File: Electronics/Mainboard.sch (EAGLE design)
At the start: 14 parts, among them IC1 4081N, T1 BC547, T2 BC547

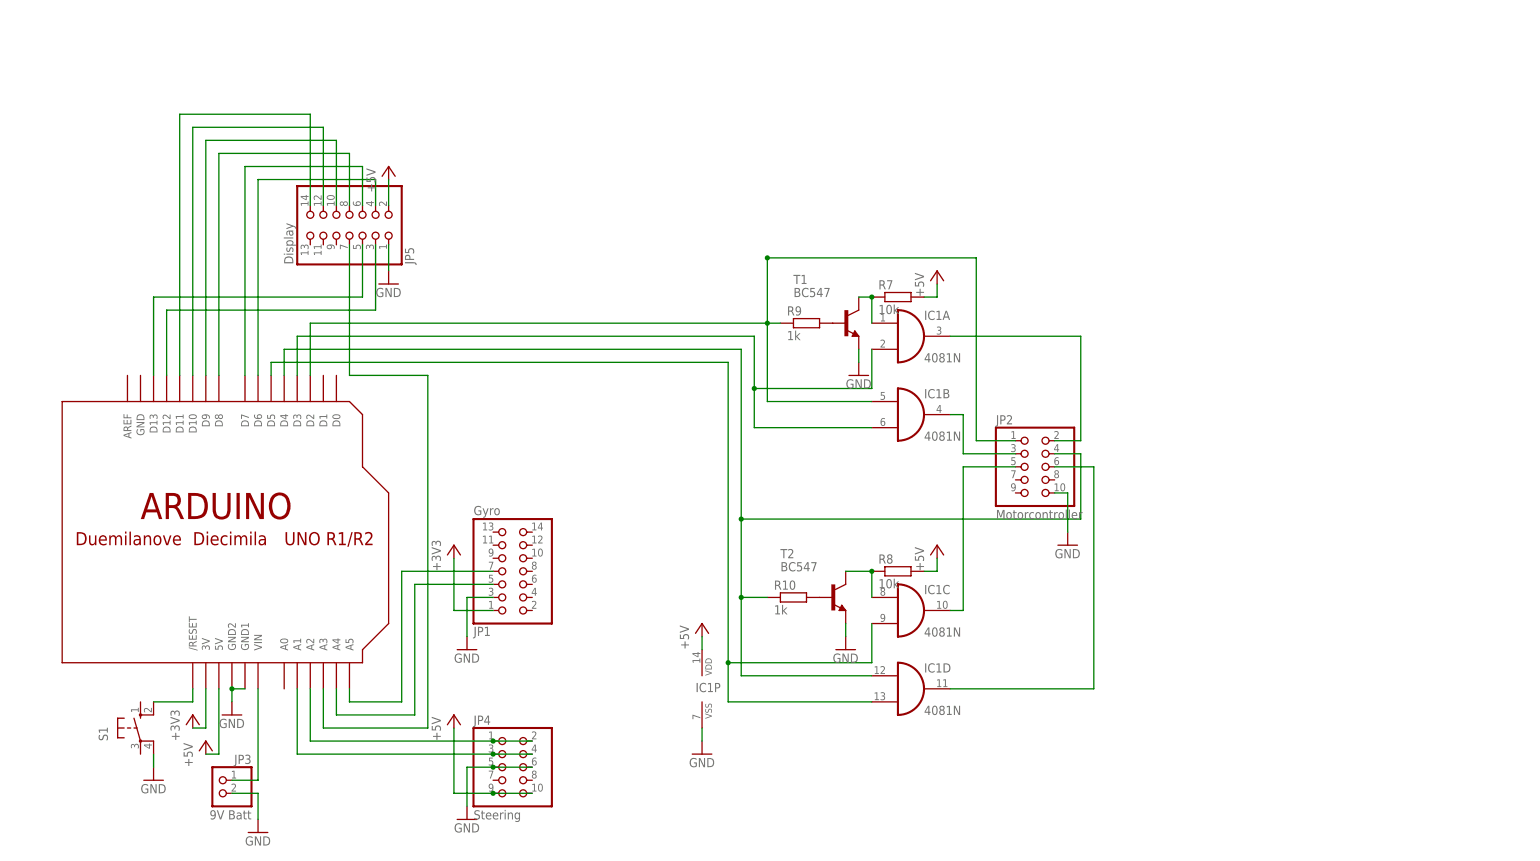
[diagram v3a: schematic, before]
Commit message: New mainboard. Closes #13, closes #21 and closes #9 as it becomes irrelevant.
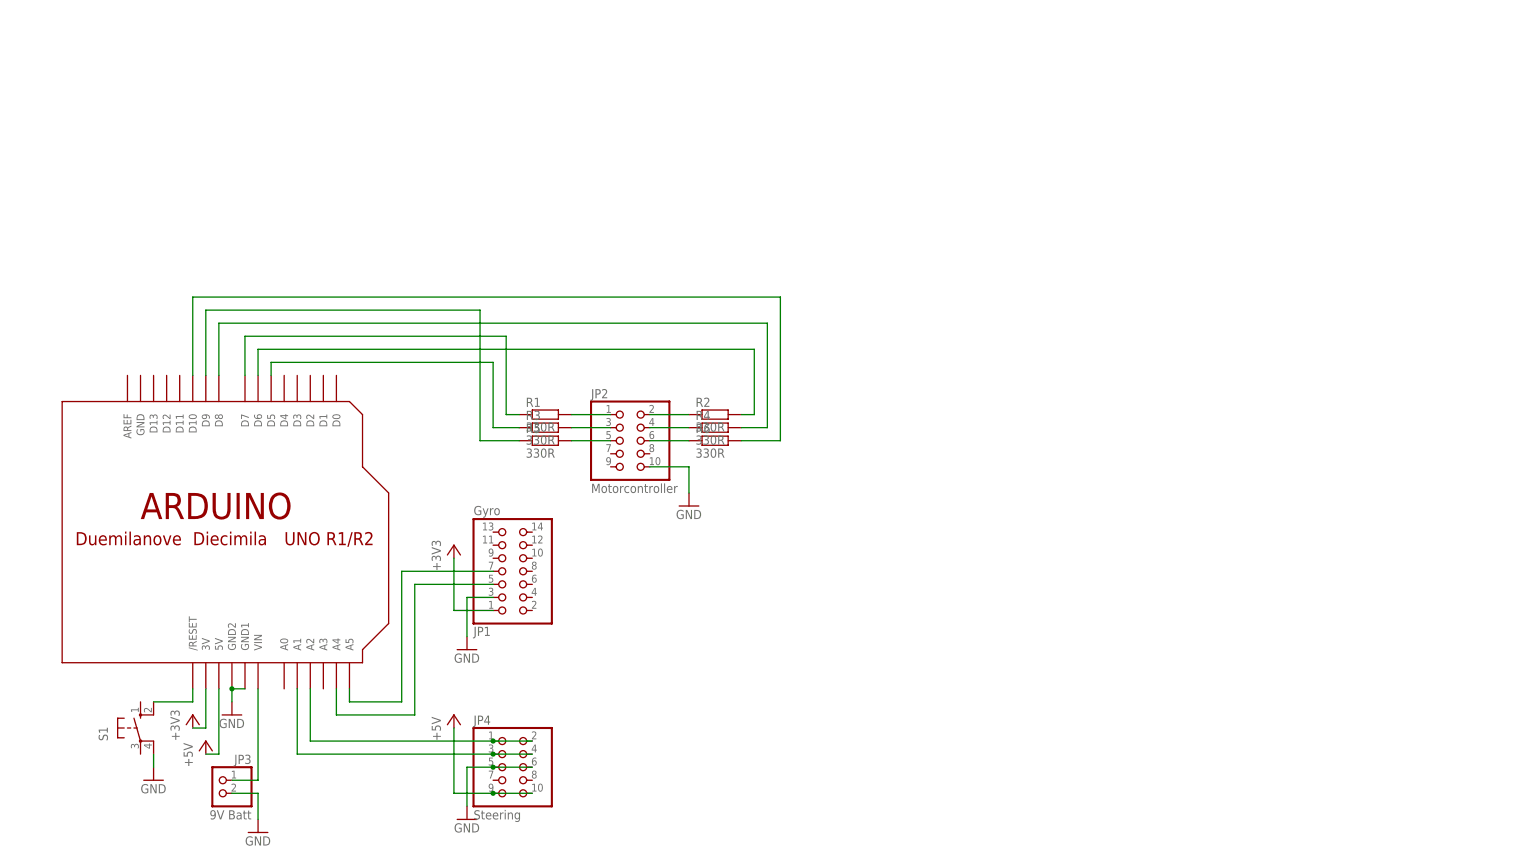
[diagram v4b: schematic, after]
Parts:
- removed IC1: 4081N, 40xx:4081N
- removed JP5: Display, pinhead:PINHD-2X7
- removed R10, R9: 1k, rcl:R-EU_0207/10
- removed R7, R8: 10k, rcl:R-EU_0207/10
- removed T1, T2: BC547, transistor:BC547
- added R1, R2, R3, R4, R5, R6: 330R, rcl:R-EU_0207/10
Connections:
- removed net N$20: R10.2, T2.B
- removed net N$31: JP5.4, U$1.D6
- removed net N$37: JP5.6, U$1.D7
- removed net N$38: JP5.8, U$1.D8
- removed net N$40: JP5.10, U$1.D9
- removed net N$42: JP5.12, U$1.D10
- removed net N$43: JP5.14, U$1.D11
- removed net N$44: JP5.3, U$1.D12
- removed net N$45: JP5.5, U$1.D13
- removed net N$46: JP5.7, U$1.A3
- new net N$6: JP2.6, R6.1
- net +5V: no longer IC1P.VDD, JP5.2, R7.2, R8.2
- net GND: no longer IC1P.VSS, JP5.1, T1.E, T2.E
- net N$1: now also JP2.1, R1.2; no longer IC1A.O, JP2.2
- net N$10: now also R2.2, U$1.D6; no longer IC1B.I0, JP2.1, R9.1, U$1.D2
- net N$11: now also R4.2, U$1.D8; no longer IC1A.I1, IC1B.I1, U$1.D3
- net N$16: now also R5.1, U$1.D9; no longer IC1C.I0, R8.1, T2.C
- net N$17: now also R6.2, U$1.D10; no longer R9.2, T1.B
- net N$2: now also R3.2; no longer IC1B.O
- net N$3: now also JP2.5, R5.2; no longer IC1D.I0, JP2.4, R10.1, U$1.D4
- net N$4: now also JP2.2, R2.1; no longer IC1C.O, JP2.5
- net N$5: now also JP2.4, R4.1; no longer IC1D.O, JP2.6
- net N$7: now also R1.1, U$1.D7; no longer IC1C.I1, IC1D.I1, U$1.D5
- net N$8: now also R3.1, U$1.D5; no longer IC1A.I0, R7.1, T1.C
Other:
- moved on the sheet: JP2

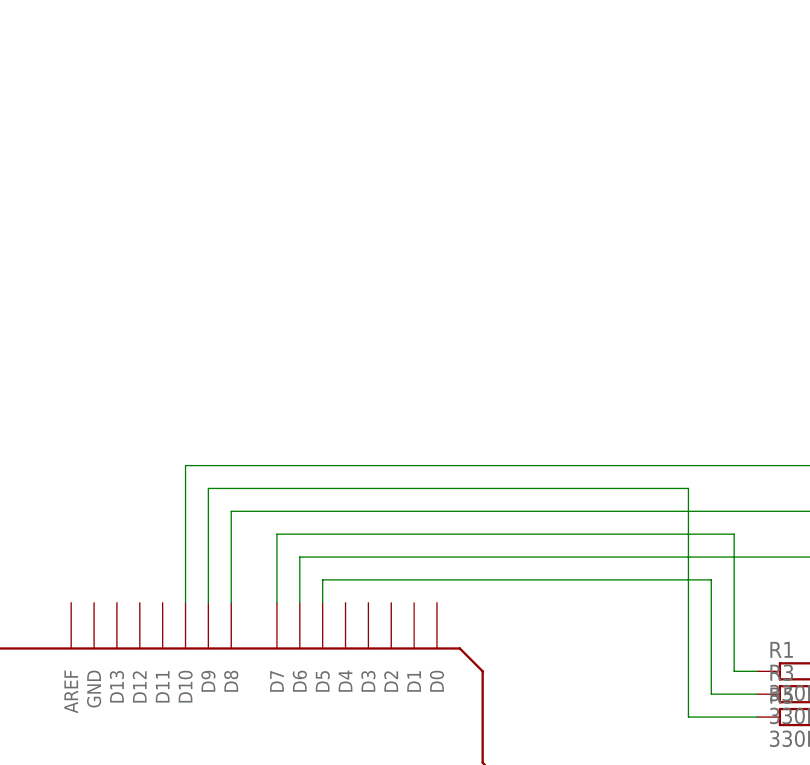
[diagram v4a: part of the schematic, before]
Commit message: Radio on mainboard. Closes #29
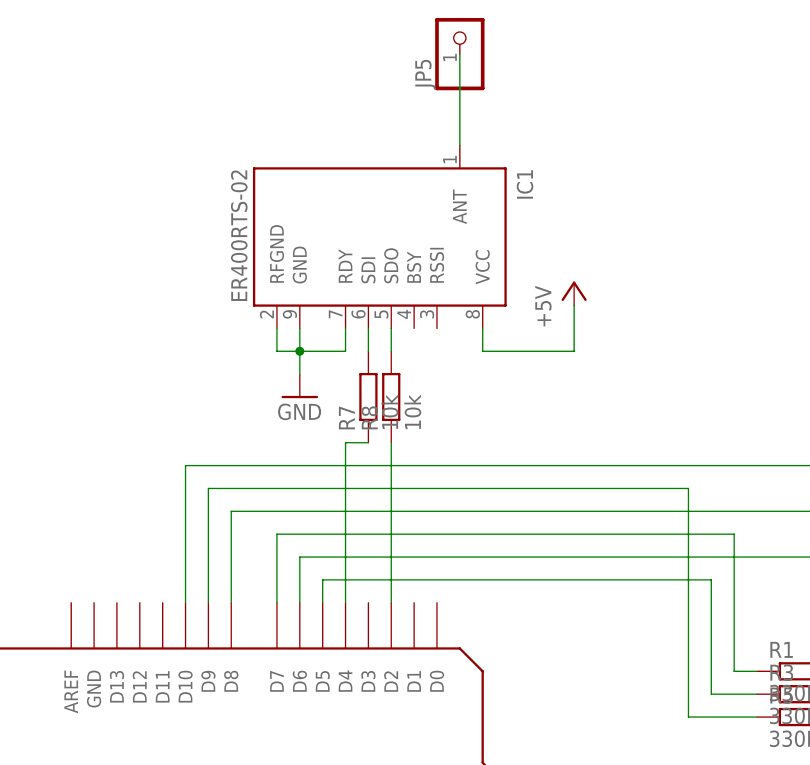
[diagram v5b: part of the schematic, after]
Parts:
- added IC1: ER400RTS-02, lprs:ER400RTS-02
- added JP5: (no value), adafruit:PINHD-1X1
- added R7, R8: 10k, rcl:R-EU_0207/10
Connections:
- new net N$12: R7.1, U$1.D4
- new net N$18: IC1.SDO, R8.2
- new net N$19: IC1.SDI, R7.2
- new net N$21: IC1.ANT, JP5.1
- new net N$9: R8.1, U$1.D2
- net +5V: now also IC1.VCC
- net GND: now also IC1.GND, IC1.RDY, IC1.RFGND
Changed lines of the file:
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@@
 <part name="R5" library="rcl" deviceset="R-EU_" device="0207/10" value="330R"/>
 <part name="R6" library="rcl" deviceset="R-EU_" device="0207/10" value="330R"/>
+<part name="IC1" library="lprs" deviceset="ER*00RTS-02" device="" technology="4"/>
+<part name="GND4" library="supply1" deviceset="GND" device=""/>
+<part name="R7" library="rcl" deviceset="R-EU_" device="0207/10" value="10k"/>
+<part name="R8" library="rcl" deviceset="R-EU_" device="0207/10" value="10k"/>
+<part name="P+1" library="supply1" deviceset="+5V" device=""/>
+<part name="JP5" library="adafruit" deviceset="PINHD-1X1" device=""/>
 </parts>
 <sheets>
@@
 <instance part="R5" gate="G$1" x="60.96" y="88.9"/>
 <instance part="R6" gate="G$1" x="93.98" y="88.9"/>
+<instance part="IC1" gate="G$1" x="12.7" y="142.24" rot="R270"/>
+<instance part="GND4" gate="1" x="5.08" y="124.46"/>
+<instance part="R7" gate="G$1" x="12.7" y="124.46" rot="R90"/>
+<instance part="R8" gate="G$1" x="15.24" y="124.46" rot="R90"/>
+<instance part="P+1" gate="1" x="35.56" y="137.16"/>
+<instance part="JP5" gate="G$1" x="22.86" y="165.1" rot="R90"/>
 </instances>
 <busses>
@@
 <wire x1="-15.24" y1="25.4" x2="-15.24" y2="27.94" width="0.1524" layer="91"/>
 </segment>
+<segment>
+<pinref part="GND4" gate="1" pin="GND"/>
+<pinref part="IC1" gate="G$1" pin="GND"/>
+<wire x1="5.08" y1="127" x2="5.08" y2="129.54" width="0.1524" layer="91"/>
+<wire x1="5.08" y1="129.54" x2="5.08" y2="132.08" width="0.1524" layer="91"/>
+<pinref part="IC1" gate="G$1" pin="RDY"/>
+<wire x1="10.16" y1="132.08" x2="10.16" y2="129.54" width="0.1524" layer="91"/>
+<wire x1="10.16" y1="129.54" x2="5.08" y2="129.54" width="0.1524" layer="91"/>
+<junction x="5.08" y="129.54"/>
+<pinref part="IC1" gate="G$1" pin="RFGND"/>
+<wire x1="2.54" y1="132.08" x2="2.54" y2="129.54" width="0.1524" layer="91"/>
+<wire x1="2.54" y1="129.54" x2="5.08" y2="129.54" width="0.1524" layer="91"/>
+</segment>
 </net>
 <net name="N$26" class="0">
@@
 <junction x="50.8" y="20.32"/>
 </segment>
+<segment>
+<pinref part="IC1" gate="G$1" pin="VCC"/>
+<wire x1="25.4" y1="132.08" x2="25.4" y2="129.54" width="0.1524" layer="91"/>
+<wire x1="25.4" y1="129.54" x2="35.56" y2="129.54" width="0.1524" layer="91"/>
+<pinref part="P+1" gate="1" pin="+5V"/>
+<wire x1="35.56" y1="129.54" x2="35.56" y2="134.62" width="0.1524" layer="91"/>
+</segment>
 </net>
 <net name="N$13" class="0">
@@
 </segment>
 </net>
+<net name="N$12" class="0">
+<segment>
+<wire x1="12.7" y1="119.38" x2="10.16" y2="119.38" width="0.1524" layer="91"/>
+<pinref part="U$1" gate="G$1" pin="D4"/>
+<wire x1="10.16" y1="119.38" x2="10.16" y2="101.6" width="0.1524" layer="91"/>
+<pinref part="R7" gate="G$1" pin="1"/>
+</segment>
+</net>
+<net name="N$9" class="0">
+<segment>
+<pinref part="U$1" gate="G$1" pin="D2"/>
+<pinref part="R8" gate="G$1" pin="1"/>
+<wire x1="15.24" y1="101.6" x2="15.24" y2="119.38" width="0.1524" layer="91"/>
+</segment>
+</net>
+<net name="N$18" class="0">
+<segment>
+<pinref part="R8" gate="G$1" pin="2"/>
+<pinref part="IC1" gate="G$1" pin="SDO"/>
+<wire x1="15.24" y1="129.54" x2="15.24" y2="132.08" width="0.1524" layer="91"/>
+</segment>
+</net>
+<net name="N$19" class="0">
+<segment>
+<pinref part="R7" gate="G$1" pin="2"/>
+<pinref part="IC1" gate="G$1" pin="SDI"/>
+<wire x1="12.7" y1="129.54" x2="12.7" y2="132.08" width="0.1524" layer="91"/>
+</segment>
+</net>
+<net name="N$21" class="0">
+<segment>
+<pinref part="JP5" gate="G$1" pin="1"/>
+<pinref part="IC1" gate="G$1" pin="ANT"/>
+<wire x1="22.86" y1="162.56" x2="22.86" y2="152.4" width="0.1524" layer="91"/>
+</segment>
+</net>

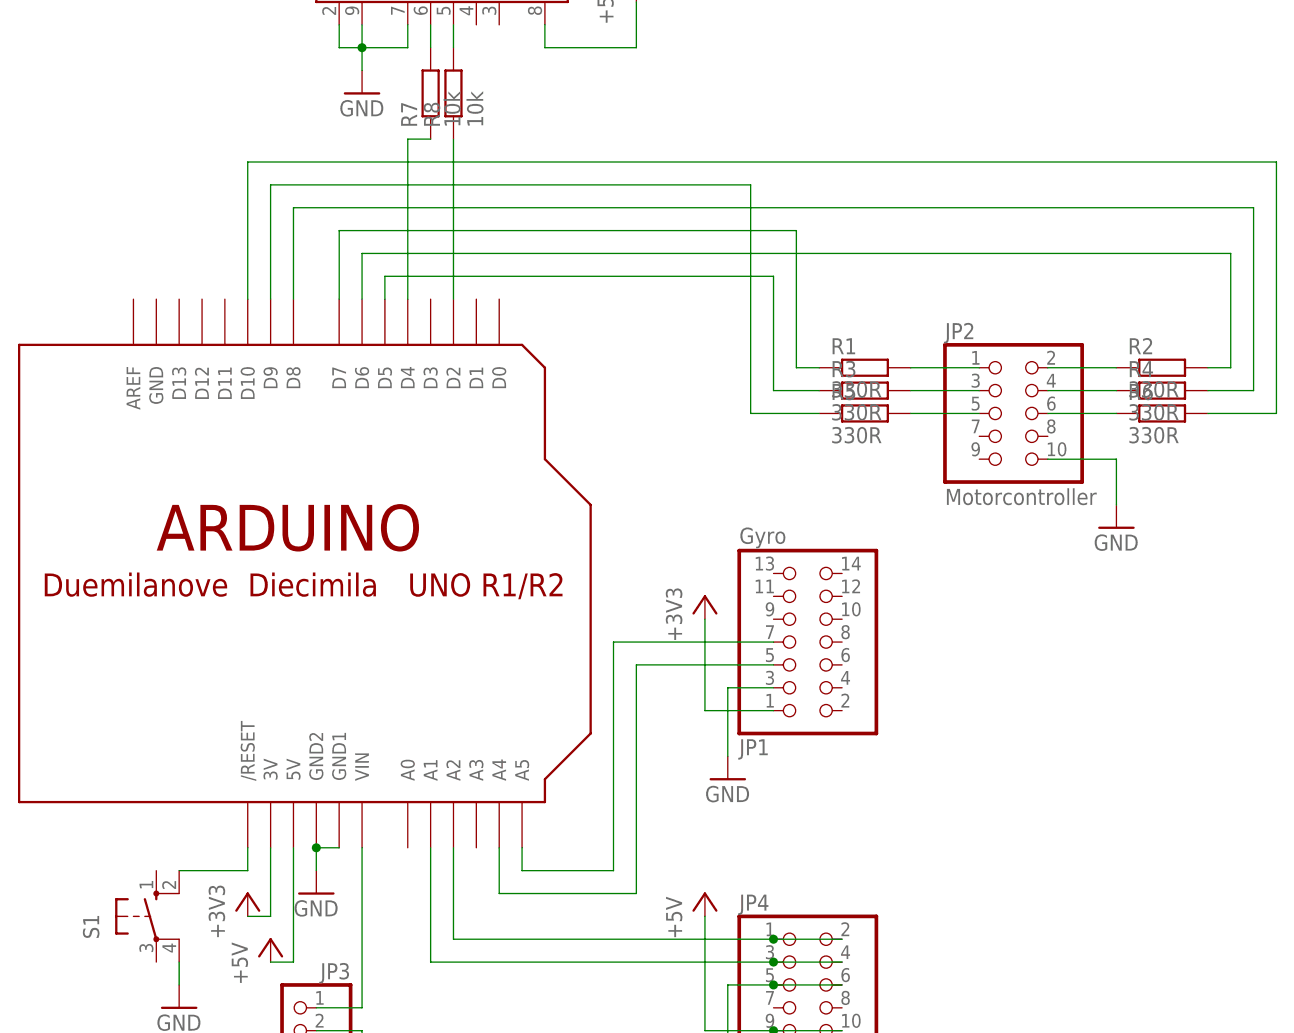
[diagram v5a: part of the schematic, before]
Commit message: Moved resistors to Motorboard. Closes #37
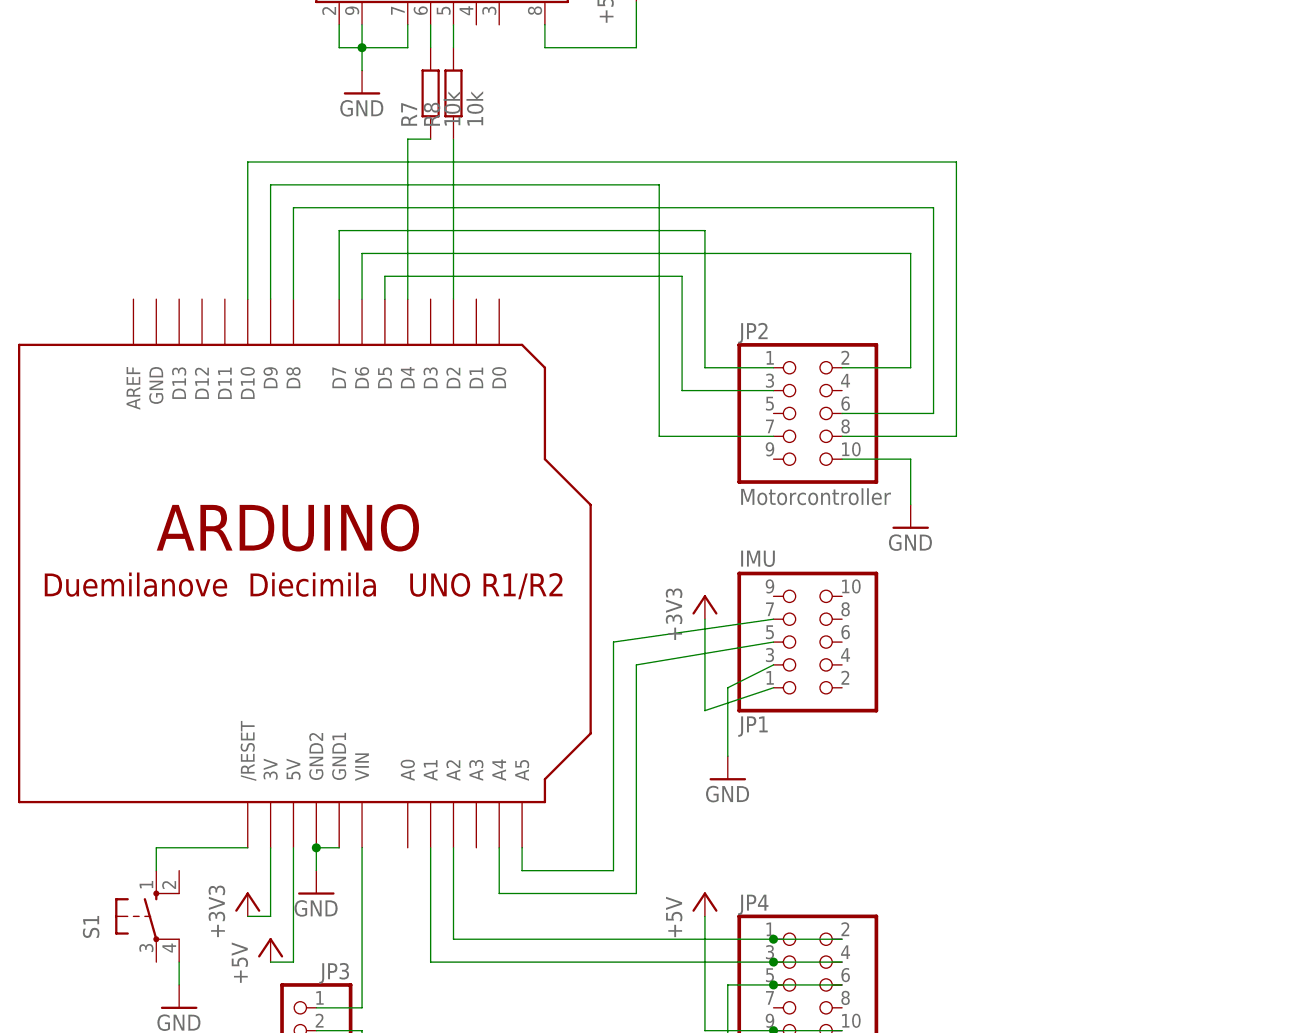
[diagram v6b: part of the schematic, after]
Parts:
- removed R1, R2, R3, R4, R5, R6: 330R, rcl:R-EU_0207/10
- JP1: value Gyro -> IMU; device pinhead:PINHD-2X7 -> pinhead:PINHD-2X5
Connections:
- removed net N$10: R2.2, U$1.D6
- removed net N$11: R4.2, U$1.D8
- removed net N$17: R6.2, U$1.D10
- removed net N$2: JP2.3, R3.2
- removed net N$3: JP2.5, R5.2
- removed net N$7: R1.1, U$1.D7
- net N$1: now also U$1.D7; no longer R1.2
- net N$15: now also S1.S; no longer S1.S1
- net N$16: now also JP2.7; no longer R5.1
- net N$4: now also U$1.D6; no longer R2.1
- net N$5: now also JP2.6, U$1.D8; no longer JP2.4, R4.1
- net N$6: now also JP2.8, U$1.D10; no longer JP2.6, R6.1
- net N$8: now also JP2.3; no longer R3.1
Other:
- moved on the sheet: JP2
